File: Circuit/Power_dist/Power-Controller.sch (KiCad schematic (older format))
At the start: 42 parts, among them P15 USB_B, U1 93LC56BT-I/OT, U2 FT232H, U3 ACPL-247-500E, U4 ACPL-247-500E, Y1 12MHz

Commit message: refactor Power_dist
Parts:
- JP2: value Jumper -> Manual_Software_Switch
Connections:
- net labels added: GNDPWR
- net labels removed: GND
- wire segments 164 -> 166
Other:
- moved on the sheet: JP2
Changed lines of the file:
@@
 L Jumper JP2
 U 1 1 5A39A4D1
-P 7350 1250
-F 0 "JP2" H 7350 1400 50  0000 C CNN
-F 1 "Jumper" H 7350 1170 50  0000 C CNN
-F 2 "Pin_Headers:Pin_Header_Straight_1x02_Pitch2.54mm" H 7350 1250 50  0001 C CNN
-F 3 "" H 7350 1250 50  0001 C CNN
-	1    7350 1250
-	0    -1   -1   0
+P 6850 1250
+F 0 "JP2" H 6850 1400 50  0000 C CNN
+F 1 "Manual_Software_Switch" H 6850 1170 50  0000 C CNN
+F 2 "Pin_Headers:Pin_Header_Straight_1x02_Pitch2.54mm" H 6850 1250 50  0001 C CNN
+F 3 "" H 6850 1250 50  0001 C CNN
+	1    6850 1250
+	1    0    0    -1
 $EndComp
 $Comp
 L +3.3V #PWR070
 U 1 1 5A39A78A
-P 7350 900
-F 0 "#PWR070" H 7350 750 50  0001 C CNN
-F 1 "+3.3V" H 7350 1040 50  0000 C CNN
-F 2 "" H 7350 900 50  0000 C CNN
-F 3 "" H 7350 900 50  0000 C CNN
-	1    7350 900
+P 6450 1050
+F 0 "#PWR070" H 6450 900 50  0001 C CNN
+F 1 "+3.3V" H 6450 1190 50  0000 C CNN
+F 2 "" H 6450 1050 50  0000 C CNN
+F 3 "" H 6450 1050 50  0000 C CNN
+	1    6450 1050
 	1    0    0    -1
 $EndComp
-Wire Wire Line
-	7350 900  7350 950
 Wire Wire Line
 	7350 2100 7500 2100
@@
 	7350 5500 7500 5500
 Connection ~ 7350 4400
-$Comp
-L GND #PWR071
-U 1 1 5A39B1A7
-P 8600 2400
-F 0 "#PWR071" H 8600 2150 50  0001 C CNN
-F 1 "GND" H 8600 2250 50  0000 C CNN
-F 2 "" H 8600 2400 50  0001 C CNN
-F 3 "" H 8600 2400 50  0001 C CNN
-	1    8600 2400
-	1    0    0    -1
-$EndComp
-$Comp
-L GND #PWR072
-U 1 1 5A39B279
-P 8600 3500
-F 0 "#PWR072" H 8600 3250 50  0001 C CNN
-F 1 "GND" H 8600 3350 50  0000 C CNN
-F 2 "" H 8600 3500 50  0001 C CNN
-F 3 "" H 8600 3500 50  0001 C CNN
-	1    8600 3500
-	1    0    0    -1
-$EndComp
-$Comp
-L GND #PWR073
-U 1 1 5A39B314
-P 8600 4700
-F 0 "#PWR073" H 8600 4450 50  0001 C CNN
-F 1 "GND" H 8600 4550 50  0000 C CNN
-F 2 "" H 8600 4700 50  0001 C CNN
-F 3 "" H 8600 4700 50  0001 C CNN
-	1    8600 4700
-	1    0    0    -1
-$EndComp
-$Comp
-L GND #PWR074
-U 1 1 5A39B4CF
-P 8600 5800
-F 0 "#PWR074" H 8600 5550 50  0001 C CNN
-F 1 "GND" H 8600 5650 50  0000 C CNN
-F 2 "" H 8600 5800 50  0001 C CNN
-F 3 "" H 8600 5800 50  0001 C CNN
-	1    8600 5800
-	1    0    0    -1
-$EndComp
 Wire Wire Line
 	8450 5700 8600 5700
@@
 	8600 2300 8600 2400
 Wire Wire Line
-	7350 1550 7350 5500
+	7350 1250 7350 5500
 Text HLabel 8450 2100 2    60   Input ~ 0
 SW1_C
@@
 Text GLabel 3150 3550 0    60   Input ~ 0
 D+
+$Comp
+L GNDPWR #PWR?
+U 1 1 5B5BEE7C
+P 8600 2400
+F 0 "#PWR?" H 8600 2200 50  0001 C CNN
+F 1 "GNDPWR" H 8600 2270 50  0000 C CNN
+F 2 "" H 8600 2350 50  0001 C CNN
+F 3 "" H 8600 2350 50  0001 C CNN
+	1    8600 2400
+	1    0    0    -1
+$EndComp
+$Comp
+L GNDPWR #PWR?
+U 1 1 5B5BEF1E
+P 8600 3500
+F 0 "#PWR?" H 8600 3300 50  0001 C CNN
+F 1 "GNDPWR" H 8600 3370 50  0000 C CNN
+F 2 "" H 8600 3450 50  0001 C CNN
+F 3 "" H 8600 3450 50  0001 C CNN
+	1    8600 3500
+	1    0    0    -1
+$EndComp
+$Comp
+L GNDPWR #PWR?
+U 1 1 5B5BF354
+P 8600 4700
+F 0 "#PWR?" H 8600 4500 50  0001 C CNN
+F 1 "GNDPWR" H 8600 4570 50  0000 C CNN
+F 2 "" H 8600 4650 50  0001 C CNN
+F 3 "" H 8600 4650 50  0001 C CNN
+	1    8600 4700
+	1    0    0    -1
+$EndComp
+$Comp
+L GNDPWR #PWR?
+U 1 1 5B5C006E
+P 8600 5800
+F 0 "#PWR?" H 8600 5600 50  0001 C CNN
+F 1 "GNDPWR" H 8600 5670 50  0000 C CNN
+F 2 "" H 8600 5750 50  0001 C CNN
+F 3 "" H 8600 5750 50  0001 C CNN
+	1    8600 5800
+	1    0    0    -1
+$EndComp
+Wire Wire Line
+	7150 1250 7350 1250
+Wire Wire Line
+	6550 1250 6450 1250
+Wire Wire Line
+	6450 1250 6450 1050
 $EndSCHEMATC

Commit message: Thruster_SW3 could be controlled
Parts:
- added R?: 150, Resistors_SMD:R_0603_HandSoldering, symbol R
- added R?: 330, Resistors_SMD:R_0603_HandSoldering, symbol R
- added U? (x2): ACPL-247-500E, symbol ACPL-247-500E
- R25, R26, R27, R28: value 150 -> 330
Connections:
- net labels added: +PWR, SW5_C, SW5_E
- wire segments 166 -> 175
- no-connect marks 15 -> 14
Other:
- moved on the sheet: JP2, R22, R23, R24, R25, R26, R27, R28, R9'1, U3A, U3B, U3C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

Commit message: changed crystal of Power_Controller in Power_dist to ABM3
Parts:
- Y1: footprint Crystals:Crystal_SMD_FOX_FE-2pin_7.5x5.0mm -> Crystals:Crystal_SMD_Abracon_ABM3-2pin_5.0x3.2mm
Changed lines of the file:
@@
 F 0 "Y1" H 4450 5750 50  0000 C CNN
 F 1 "12MHz" H 4450 5550 50  0000 C CNN
-F 2 "Crystals:Crystal_SMD_FOX_FE-2pin_7.5x5.0mm" H 4450 5650 60  0001 C CNN
+F 2 "Crystals:Crystal_SMD_Abracon_ABM3-2pin_5.0x3.2mm" H 4450 5650 60  0001 C CNN
 F 3 "" H 4450 5650 60  0000 C CNN
 	1    4450 5650

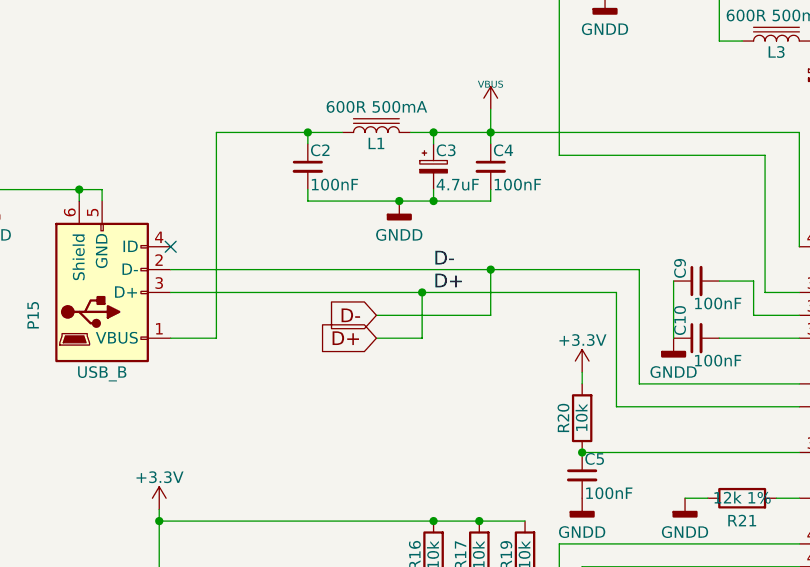
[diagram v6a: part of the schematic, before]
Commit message: added 10R to data+ and data- of FT232 in Power_Controller on Power_dist
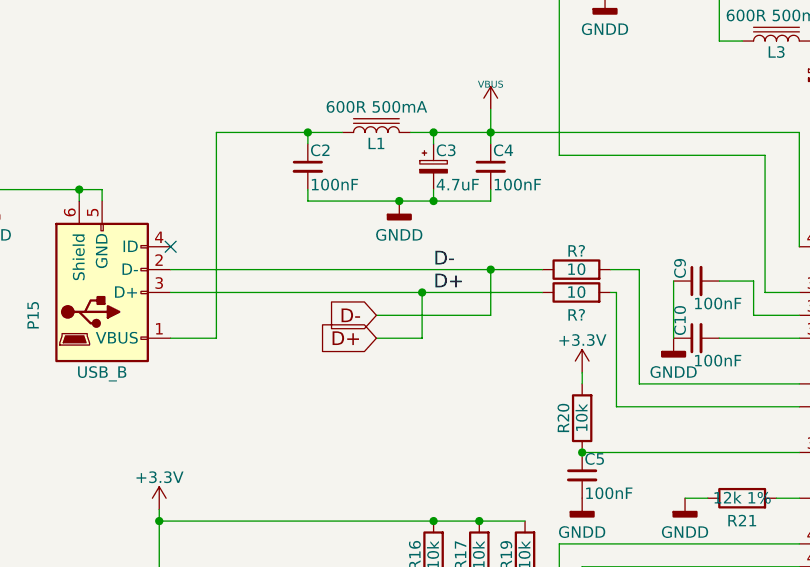
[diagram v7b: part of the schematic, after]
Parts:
- added R? (x2): 10, Resistors_SMD:R_0603_HandSoldering, symbol R
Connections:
- wire segments 175 -> 177
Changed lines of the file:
@@
 Connection ~ 3400 2650
 Wire Wire Line
-	2250 3350 4200 3350
-Wire Wire Line
 	4200 3350 4200 3850
-Wire Wire Line
-	2250 3250 4300 3250
 Wire Wire Line
 	4300 3250 4300 3750
@@
 Text HLabel 10300 4425 2    60   UnSpc ~ 0
 SW5_C
+$Comp
+L R R?
+U 1 1 5B50FC60
+P 4025 3250
+F 0 "R?" V 4105 3250 50  0000 C CNN
+F 1 "10" V 4025 3250 50  0000 C CNN
+F 2 "Resistors_SMD:R_0603_HandSoldering" V 3955 3250 30  0001 C CNN
+F 3 "" H 4025 3250 30  0000 C CNN
+	1    4025 3250
+	0    -1   -1   0
+$EndComp
+Wire Wire Line
+	4175 3250 4300 3250
+Wire Wire Line
+	2250 3250 3875 3250
+$Comp
+L R R?
+U 1 1 5B512710
+P 4025 3350
+F 0 "R?" V 3925 3350 50  0000 C CNN
+F 1 "10" V 4025 3350 50  0000 C CNN
+F 2 "Resistors_SMD:R_0603_HandSoldering" V 3955 3350 30  0001 C CNN
+F 3 "" H 4025 3350 30  0000 C CNN
+	1    4025 3350
+	0    -1   -1   0
+$EndComp
+Wire Wire Line
+	4200 3350 4175 3350
+Wire Wire Line
+	2250 3350 3875 3350
 $EndSCHEMATC
